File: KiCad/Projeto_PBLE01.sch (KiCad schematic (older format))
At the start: 36 parts

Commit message: começo da pcb
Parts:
- D1, D3, D4, D_PWR_GREEN1, Escrita_USB1, Leitura_USB1: footprint LED_SMD:LED_1206_3216Metric -> LED_SMD:LED_1206_3216Metric_Pad1.42x1.75mm_HandSolder
- D2: footprint LED_SMD:LED_1206_3216Metric_Castellated -> LED_SMD:LED_1206_3216Metric_Pad1.42x1.75mm_HandSolder
- Led_Control1: footprint Button_Switch_THT:DIP4PIN -> My_Lib:DIP4PIN
- PWR_Source1: footprint Connector_BarrelJack:PJ-002A -> My_Lib:PJ-002A
- Reset_Button1: footprint Resistor_SMD:R_0805_2012Metric -> Button_Switch_THT:SW_PUSH_6mm
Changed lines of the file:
@@
 F 0 "Leitura_USB1" H 10443 3787 50  0000 C CNN
 F 1 "LED" H 10443 3786 50  0001 C CNN
-F 2 "LED_SMD:LED_1206_3216Metric" H 10450 3950 50  0001 C CNN
+F 2 "LED_SMD:LED_1206_3216Metric_Pad1.42x1.75mm_HandSolder" H 10450 3950 50  0001 C CNN
 F 3 "~" H 10450 3950 50  0001 C CNN
 	1    10450 3950
@@
 F 0 "Escrita_USB1" H 10443 4087 50  0000 C CNN
 F 1 "LED" H 10443 4086 50  0001 C CNN
-F 2 "LED_SMD:LED_1206_3216Metric" H 10450 4250 50  0001 C CNN
+F 2 "LED_SMD:LED_1206_3216Metric_Pad1.42x1.75mm_HandSolder" H 10450 4250 50  0001 C CNN
 F 3 "~" H 10450 4250 50  0001 C CNN
 	1    10450 4250
@@
 F 0 "D3" H 10443 5087 50  0000 C CNN
 F 1 "LED" H 10443 5086 50  0001 C CNN
-F 2 "LED_SMD:LED_1206_3216Metric" H 10450 5250 50  0001 C CNN
+F 2 "LED_SMD:LED_1206_3216Metric_Pad1.42x1.75mm_HandSolder" H 10450 5250 50  0001 C CNN
 F 3 "~" H 10450 5250 50  0001 C CNN
 	1    10450 5250
@@
 F 0 "D4" H 10443 5387 50  0000 C CNN
 F 1 "LED" H 10443 5386 50  0001 C CNN
-F 2 "LED_SMD:LED_1206_3216Metric" H 10450 5550 50  0001 C CNN
+F 2 "LED_SMD:LED_1206_3216Metric_Pad1.42x1.75mm_HandSolder" H 10450 5550 50  0001 C CNN
 F 3 "~" H 10450 5550 50  0001 C CNN
 	1    10450 5550
@@
 F 0 "D_PWR_GREEN1" H 10443 5787 50  0000 C CNN
 F 1 "G_LED" H 10443 5786 50  0001 C CNN
-F 2 "LED_SMD:LED_1206_3216Metric" H 10450 5950 50  0001 C CNN
+F 2 "LED_SMD:LED_1206_3216Metric_Pad1.42x1.75mm_HandSolder" H 10450 5950 50  0001 C CNN
 F 3 "~" H 10450 5950 50  0001 C CNN
 	1    10450 5950
@@
 F 0 "PWR_Source1" H 1057 7525 50  0000 C CNN
 F 1 "Jack-DC" H 1057 7434 50  0001 C CNN
-F 2 "Connector_BarrelJack:PJ-002A" H 1050 7160 50  0001 C CNN
+F 2 "My_Lib:PJ-002A" H 1050 7160 50  0001 C CNN
 F 3 "~" H 1050 7160 50  0001 C CNN
 	1    1000 7200
@@
 F 0 "Reset_Button1" V 8200 5998 50  0000 L CNN
 F 1 "SW_Push" V 8245 5998 50  0001 L CNN
-F 2 "Resistor_SMD:R_0805_2012Metric" H 8200 6050 50  0001 C CNN
+F 2 "Button_Switch_THT:SW_PUSH_6mm" H 8200 6050 50  0001 C CNN
 F 3 "~" H 8200 6050 50  0001 C CNN
 	1    8200 5850
@@
 F 0 "D1" H 10443 4487 50  0000 C CNN
 F 1 "LED" H 10443 4486 50  0001 C CNN
-F 2 "LED_SMD:LED_1206_3216Metric" H 10450 4650 50  0001 C CNN
+F 2 "LED_SMD:LED_1206_3216Metric_Pad1.42x1.75mm_HandSolder" H 10450 4650 50  0001 C CNN
 F 3 "~" H 10450 4650 50  0001 C CNN
 	1    10450 4650
@@
 F 0 "D2" H 10443 4787 50  0000 C CNN
 F 1 "LED" H 10443 4786 50  0001 C CNN
-F 2 "LED_SMD:LED_1206_3216Metric_Castellated" H 10450 4950 50  0001 C CNN
+F 2 "LED_SMD:LED_1206_3216Metric_Pad1.42x1.75mm_HandSolder" H 10450 4950 50  0001 C CNN
 F 3 "~" H 10450 4950 50  0001 C CNN
 	1    10450 4950
@@
 F 0 "Led_Control1" H 6150 4525 50  0000 C CNN
 F 1 "SW_DIP_x04" H 6150 4526 50  0001 C CNN
-F 2 "Button_Switch_THT:DIP4PIN" H 6150 4150 50  0001 C CNN
+F 2 "My_Lib:DIP4PIN" H 6150 4150 50  0001 C CNN
 F 3 "~" H 6150 4150 50  0001 C CNN
 	1    6150 4150

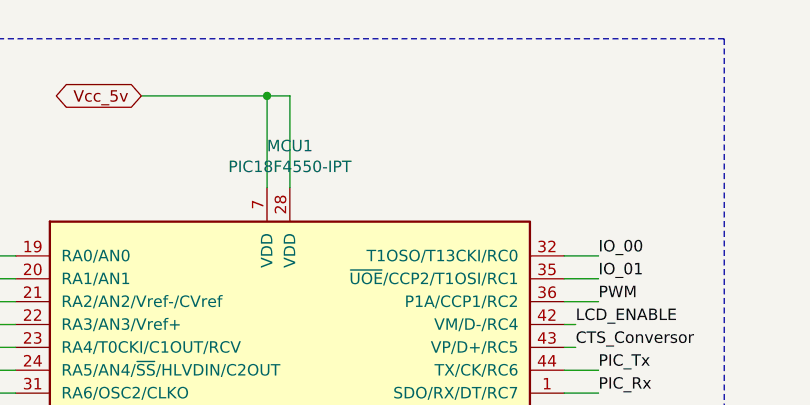
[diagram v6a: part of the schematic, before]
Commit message: correção P1: LCD e Capacitores
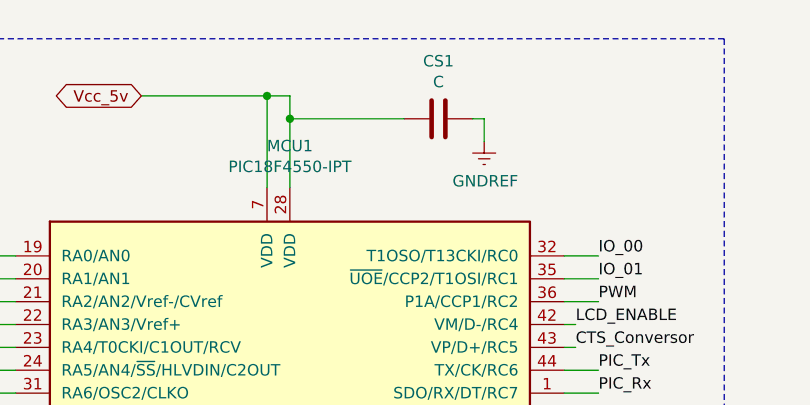
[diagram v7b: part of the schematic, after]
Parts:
- added CS1: C, Capacitor_SMD:C_0805_2012Metric_Pad1.18x1.45mm_HandSolder, symbol Device:C
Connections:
- net GNDREF: now also CS1.1
- net Vcc_5v: now also CS1.2
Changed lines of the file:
@@
 	2800 900  2900 900
 Wire Wire Line
-	2900 900  2900 1300
+	2900 900  2900 1000
 Connection ~ 2800 900
 Wire Wire Line
@@
 Wire Wire Line
 	1550 2200 1700 2200
+$Comp
+L power:GNDREF #PWR02
+U 1 1 60F6CB30
+P 3750 1100
+F 0 "#PWR02" H 3750 850 50  0001 C CNN
+F 1 "GNDREF" H 3755 927 50  0000 C CNN
+F 2 "" H 3750 1100 50  0001 C CNN
+F 3 "" H 3750 1100 50  0001 C CNN
+	1    3750 1100
+	1    0    0    -1
+$EndComp
+$Comp
+L Device:C CS1
+U 1 1 60F6DA37
+P 3550 1000
+F 0 "CS1" V 3298 1000 50  0000 C CNN
+F 1 "C" V 3389 1000 50  0000 C CNN
+F 2 "Capacitor_SMD:C_0805_2012Metric_Pad1.18x1.45mm_HandSolder" H 3588 850 50  0001 C CNN
+F 3 "~" H 3550 1000 50  0001 C CNN
+	1    3550 1000
+	0    1    1    0
+$EndComp
+Wire Wire Line
+	3750 1100 3750 1000
+Wire Wire Line
+	3750 1000 3700 1000
+Wire Wire Line
+	3400 1000 2900 1000
+Connection ~ 2900 1000
+Wire Wire Line
+	2900 1000 2900 1300
 $EndSCHEMATC

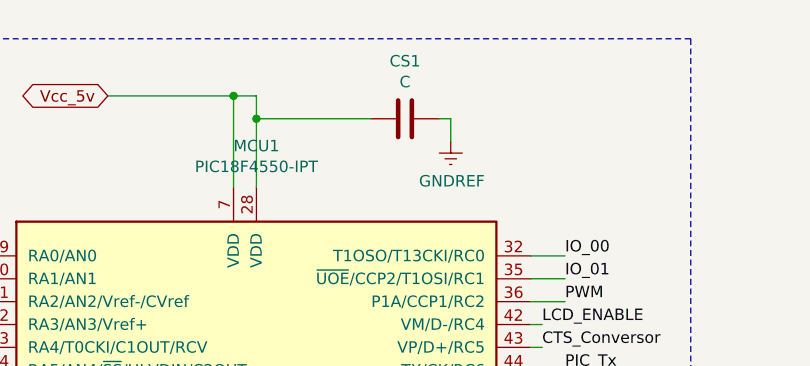
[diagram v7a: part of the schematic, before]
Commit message: Valores dos capacitores CS
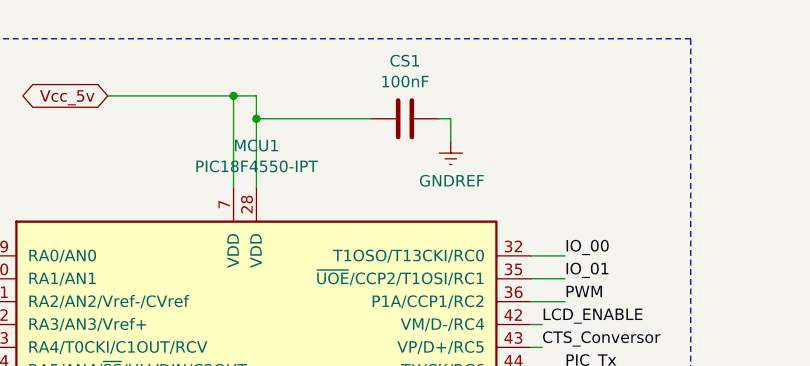
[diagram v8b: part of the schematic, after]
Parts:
- CS1: value C -> 100nF
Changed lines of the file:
@@
 P 3550 1000
 F 0 "CS1" V 3298 1000 50  0000 C CNN
-F 1 "C" V 3389 1000 50  0000 C CNN
+F 1 "100nF" V 3389 1000 50  0000 C CNN
 F 2 "Capacitor_SMD:C_0805_2012Metric_Pad1.18x1.45mm_HandSolder" H 3588 850 50  0001 C CNN
 F 3 "~" H 3550 1000 50  0001 C CNN
